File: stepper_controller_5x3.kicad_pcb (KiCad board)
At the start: 2 copper layers, 120.7 x 66 mm, 1 part

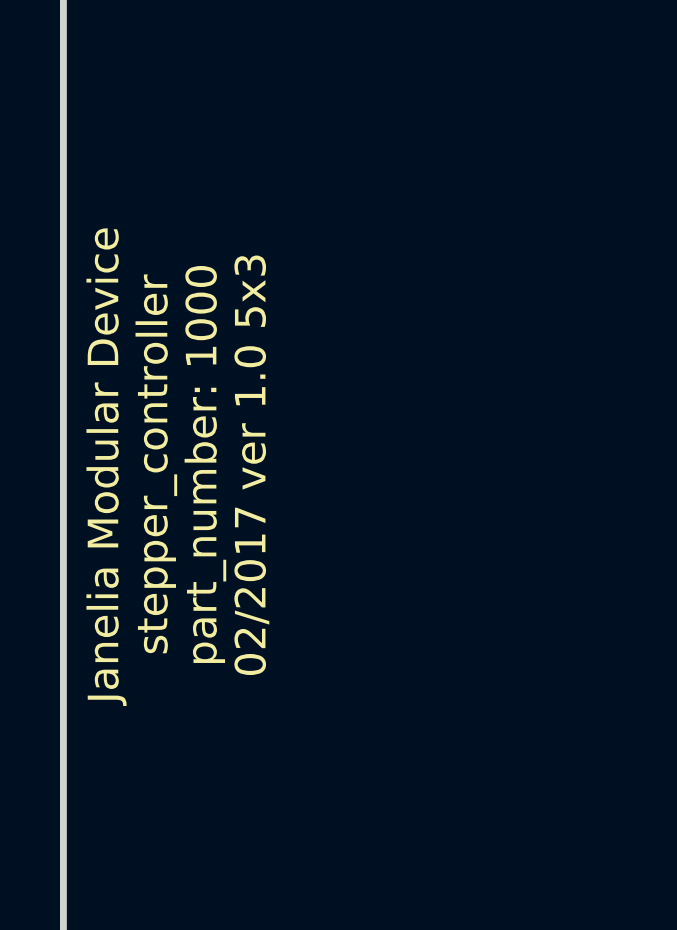
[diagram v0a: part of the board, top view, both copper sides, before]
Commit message: Added files from stepper_controller_3x2.
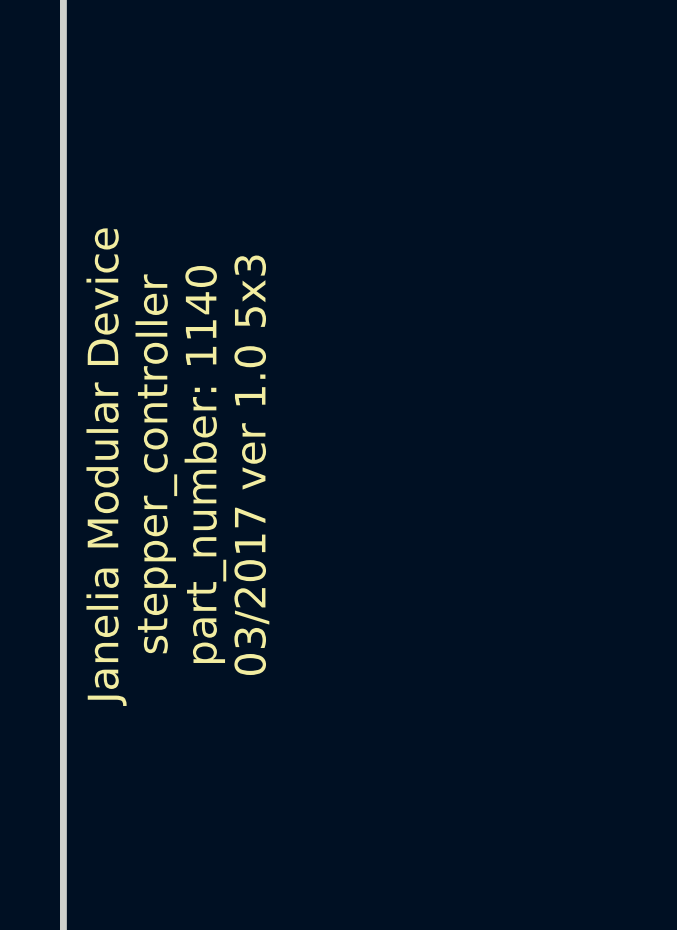
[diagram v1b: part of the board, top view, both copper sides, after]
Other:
- board text added: "Janelia Modular Device stepper_controller part_number: 1140 03/2017 ver 1.0 5x3"
- board text removed: "Janelia Modular Device stepper_controller part_number: 1000 02/2017 ver 1.0 5x3"
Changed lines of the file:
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@@
-(kicad_pcb (version 20170123) (host pcbnew no-vcs-found-7602~57~ubuntu16.04.1)
+(kicad_pcb (version 20170123) (host pcbnew no-vcs-found-40f60c9~58~ubuntu16.04.1)
   (general
     (links 0)
     (no_connects 0)
-    (area 0 0 0 0)
+    (area 69.481699 72.021699 190.868301 138.798301)
     (thickness 1.6)
     (drawings 6)
@@
     (effects (font (size 1.016 1.016) (thickness 0.1905)))
   )
-  (gr_text "Janelia Modular Device\nstepper_controller\npart_number: 1000\n02/2017 ver 1.0 5x3" (at 73.66 105.41 90) (layer F.SilkS)
+  (gr_text "Janelia Modular Device\nstepper_controller\npart_number: 1140\n03/2017 ver 1.0 5x3" (at 73.66 105.41 90) (layer F.SilkS)
     (effects (font (size 1.016 1.016) (thickness 0.254)))
   )

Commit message: Progress towards v1.0.
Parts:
- added C1: 0.1uF, stepper_controller_5x3:SM1210, F.Cu at (283.9, 127.0)
- added C10: 10uF, stepper_controller_5x3:SM1210, F.Cu at (295.1, 100.7)
- added C11: 0.1uF, stepper_controller_5x3:SM1210, F.Cu at (274.4, 102.7)
- added C2: 0.1uF, stepper_controller_5x3:SM1210, F.Cu at (282.9, 138.7)
- added C3: 100uF_POL, stepper_controller_5x3:C_ELEC_12.5, F.Cu at (79.4, 120.7)
- added C4: 10uF, stepper_controller_5x3:SM1210, F.Cu at (224.8, 100.7)
- added C5: 0.1uF, stepper_controller_5x3:SM1210, F.Cu at (204.1, 102.7)
- added C6: 100uF_POL, stepper_controller_5x3:C_ELEC_12.5, F.Cu at (112.4, 120.7)
- added C7: 10uF, stepper_controller_5x3:SM1210, F.Cu at (224.8, 141.6)
- added C8: 0.1uF, stepper_controller_5x3:SM1210, F.Cu at (204.1, 143.6)
- added C9: 100uF_POL, stepper_controller_5x3:C_ELEC_12.5, F.Cu at (145.4, 120.7)
- added CLK1: CLK_32MHZ, stepper_controller_5x3:CTS_SMD_4_7X5MM, F.Cu at (276.6, 128.5)
- added D1: diode_schottky_45V_10A, stepper_controller_5x3:CFP15, F.Cu at (281.4, 117.8)
- added P1: PWR_JACK_2.5x5.5, stepper_controller_5x3:DCJACK_2PIN_HIGHCURRENT, F.Cu at (191.1, 105.4)
- added SS1: STEPSTICK, stepper_controller_5x3:STEPSTICK, F.Cu at (95.2, 105.4)
- added SS2: STEPSTICK, stepper_controller_5x3:STEPSTICK, F.Cu at (128.3, 105.4)
- added SS3: STEPSTICK, stepper_controller_5x3:STEPSTICK, F.Cu at (161.3, 105.4)
- added T1: TERM_BLK_HDR_4POS_VERT_0.2IN, stepper_controller_5x3:TERM_BLK_HDR_4POS_VERT_0.2IN, F.Cu at (95.2, 91.4)
- added T2: TERM_BLK_HDR_4POS_VERT_0.150IN, stepper_controller_5x3:TERM_BLK_HDR_4POS_VERT_0.150IN, F.Cu at (95.2, 120.7)
- added T3: TERM_BLK_HDR_4POS_VERT_0.2IN, stepper_controller_5x3:TERM_BLK_HDR_4POS_VERT_0.2IN, F.Cu at (128.3, 91.4)
- added T4: TERM_BLK_HDR_4POS_VERT_0.150IN, stepper_controller_5x3:TERM_BLK_HDR_4POS_VERT_0.150IN, F.Cu at (128.3, 120.7)
- added T5: TERM_BLK_HDR_4POS_VERT_0.2IN, stepper_controller_5x3:TERM_BLK_HDR_4POS_VERT_0.2IN, F.Cu at (161.3, 91.4)
- added T6: TERM_BLK_HDR_4POS_VERT_0.150IN, stepper_controller_5x3:TERM_BLK_HDR_4POS_VERT_0.150IN, F.Cu at (161.3, 120.0)
- added U1: TMC429, stepper_controller_5x3:QFN-5x5-32, F.Cu at (276.1, 141.4)
- added U2: MAX6817, stepper_controller_5x3:MAX6817, F.Cu at (208.8, 101.8)
- added U3: MAX6817, stepper_controller_5x3:MAX6817, F.Cu at (208.8, 142.7)
- added U4: MAX6817, stepper_controller_5x3:MAX6817, F.Cu at (279.2, 101.8)
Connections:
- MDB1 pad 11: (no net) -> /MOSI
- MDB1 pad 12: (no net) -> /MISO
- MDB1 pad 13: (no net) -> /SCK
- MDB1 pad 15: (no net) -> /CS_429
- MDB1 pad 16: (no net) -> /CS_DRIVER_0
- MDB1 pad 17: (no net) -> /CS_DRIVER_1
- MDB1 pad 18: (no net) -> /CS_DRIVER_2
- MDB1 pad 3V3: (no net) -> +3V3
- MDB1 pad 40: (no net) -> /ENABLE_0
- MDB1 pad 41: (no net) -> /ENABLE_1
- MDB1 pad 42: (no net) -> /ENABLE_2
- MDB1 pad 5: (no net) -> /INT
- MDB1 pad 6: (no net) -> /POSCOMP
- MDB1 pad GND: (no net) -> GND
- MDB1 pad VDD: (no net) -> VDD
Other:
- board size 120.7 x 66 mm -> 121.3 x 67.3 mm
- board text added: "Janelia Modular Device stepper_controller part_number: 1140 06/2017 ver 1.0 5x3"
- board text removed: "Janelia Modular Device stepper_controller part_number: 1140 03/2017 ver 1.0 5x3"

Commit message: Finished v1.0.
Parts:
- C1, C10, C11, C2, C4, C5, C7, C8, CLK1, D1, U1, U2, U3, U4: moved to B.Cu
- C3, C6, C9: value 100uF_POL -> 220uF_POL; footprint stepper_controller_5x3:C_ELEC_12.5 -> stepper_controller_5x3:C_ELEC_10
- moved C10 203.7 mm to (91.4, 96.5)
- moved C11 182.3 mm to (94.0, 128.3), turned to 90 degrees
- moved U4 182.0 mm to (99.1, 128.3), turned to 270 degrees
- moved C2 176.5 mm to (108.0, 115.6), turned to 90 degrees
- moved U1 162.6 mm to (115.6, 115.6), turned to 180 degrees
- moved C1 151.7 mm to (132.7, 115.6), turned to 270 degrees
- moved CLK1 151.4 mm to (125.7, 115.6), turned to 180 degrees
- moved C7 110.0 mm to (124.5, 96.5)
- moved D1 104.1 mm to (179.1, 98.4)
- moved C8 78.6 mm to (127.0, 128.3), turned to 90 degrees
- moved U3 78.1 mm to (132.1, 128.3), turned to 270 degrees
- moved C3 72.7 mm to (148.6, 98.4)
- moved SS1 70.2 mm to (165.1, 98.4)
- moved T1 70.2 mm to (165.1, 84.5)
- moved T2 69.9 mm to (165.1, 123.8)
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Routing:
- net GND: track 0.00 -> 385.3 mm
- net +3V3: track 0.00 -> 308.9 mm
- net /MOSI: track 0.00 -> 150.8 mm
- net /MISO: track 0.00 -> 148.3 mm
- net VDD: track 0.00 -> 145.3 mm
- net /SCK: track 0.00 -> 138.1 mm
- net /CS_DRIVER_0: track 0.00 -> 79.8 mm
- net /ENABLE_0: track 0.00 -> 76.9 mm
- net /tmc429_driver_0/REFR_0: track 0.00 -> 74.8 mm
- net /INT: track 0.00 -> 73.6 mm, vias 0 -> 2
- net /ENABLE_2: track 0.00 -> 73.2 mm
- net /CS_DRIVER_1: track 0.00 -> 72.7 mm
- net /tmc429_driver_0/DIR_0: track 0.00 -> 71.9 mm, vias 0 -> 1
- net /tmc429_driver_0/STEP_0: track 0.00 -> 66.3 mm, vias 0 -> 1
- net /tmc429_driver_0/REF_0: track 0.00 -> 57.3 mm
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- added copper zone on B.Cu, net GND
- added copper zone on F.Cu, net VDD
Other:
- net class GND: trace_width 0.4064 -> 0.3048
- net class POWER: clearance 0.254 -> 0.1016; trace_width 0.8128 -> 0.3048
- net class SIGNAL: trace_width 0.4064 -> 0.3048
- net class SUPERPOWER: clearance 0.254 -> 0.1016; trace_width 1.2192 -> 1.27
- board text added: "0"
- board text added: "1"
- board text added: "2"
- board text added: "2.5x5.5 Center + +9-42VDC"
- board text added: "A+"
- board text added: "A-"
- board text added: "B+"
- board text added: "B-"
- board text added: "GND"
- board text added: "REF"
- board text added: "REFR"

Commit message: Progress toward v1.1.
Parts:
- added L1: 90nH, stepper_controller_5x3:ECS-MPI4040, B.Cu at (172.7, 87.8)
- added L10: 90nH, stepper_controller_5x3:ECS-MPI4040, B.Cu at (101.6, 87.8)
- added L11: 90nH, stepper_controller_5x3:ECS-MPI4040, B.Cu at (96.5, 87.8)
- added L12: 90nH, stepper_controller_5x3:ECS-MPI4040, B.Cu at (91.4, 87.8)
- added L2: 90nH, stepper_controller_5x3:ECS-MPI4040, B.Cu at (167.6, 87.8)
- added L3: 90nH, stepper_controller_5x3:ECS-MPI4040, B.Cu at (162.6, 87.8)
- added L4: 90nH, stepper_controller_5x3:ECS-MPI4040, B.Cu at (157.5, 87.8)
- added L5: 90nH, stepper_controller_5x3:ECS-MPI4040, B.Cu at (139.7, 87.8)
- added L6: 90nH, stepper_controller_5x3:ECS-MPI4040, B.Cu at (134.6, 87.8)
- added L7: 90nH, stepper_controller_5x3:ECS-MPI4040, B.Cu at (129.5, 87.8)
- added L8: 90nH, stepper_controller_5x3:ECS-MPI4040, B.Cu at (124.5, 87.8)
- added L9: 90nH, stepper_controller_5x3:ECS-MPI4040, B.Cu at (106.7, 87.8)
- added R1: 470pF, stepper_controller_5x3:SM0805, B.Cu at (172.7, 80.6)
- added R10: 470pF, stepper_controller_5x3:SM0805, B.Cu at (101.6, 80.6)
- added R11: 470pF, stepper_controller_5x3:SM0805, B.Cu at (96.5, 80.6)
- added R12: 470pF, stepper_controller_5x3:SM0805, B.Cu at (91.4, 80.6)
- added R2: 470pF, stepper_controller_5x3:SM0805, B.Cu at (167.6, 80.6)
- added R3: 470pF, stepper_controller_5x3:SM0805, B.Cu at (162.6, 80.6)
- added R4: 470pF, stepper_controller_5x3:SM0805, B.Cu at (157.5, 80.6)
- added R5: 470pF, stepper_controller_5x3:SM0805, B.Cu at (139.7, 80.6)
- added R6: 470pF, stepper_controller_5x3:SM0805, B.Cu at (134.6, 80.6)
- added R7: 470pF, stepper_controller_5x3:SM0805, B.Cu at (129.5, 80.6)
- added R8: 470pF, stepper_controller_5x3:SM0805, B.Cu at (124.5, 80.6)
- added R9: 470pF, stepper_controller_5x3:SM0805, B.Cu at (106.7, 80.6)
- moved C10 0.64 mm to (91.4, 97.2)
- moved C3 0.64 mm to (148.6, 99.1)
- moved C4 0.64 mm to (157.5, 97.2)
- moved C6 0.64 mm to (115.6, 99.1)
- moved C7 0.64 mm to (124.5, 97.2)
- moved C9 0.64 mm to (82.5, 99.1)
- moved SS1 0.64 mm to (165.1, 99.1)
- moved SS2 0.64 mm to (132.1, 99.1)
- moved SS3 0.64 mm to (99.1, 99.1)
- moved T1 0.64 mm to (165.1, 83.8)
- moved T3 0.64 mm to (132.1, 83.8)
- moved T5 0.64 mm to (99.1, 83.8)
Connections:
- MDB1 pad 14: (no net) -> Net-(MDB1-Pad14)
- MDB1 pad 19: (no net) -> Net-(MDB1-Pad19)
- MDB1 pad 2: (no net) -> Net-(MDB1-Pad2)
- MDB1 pad 20: (no net) -> Net-(MDB1-Pad20)
- MDB1 pad 21: (no net) -> Net-(MDB1-Pad21)
- MDB1 pad 22: (no net) -> Net-(MDB1-Pad22)
- MDB1 pad 23: (no net) -> Net-(MDB1-Pad23)
- MDB1 pad 29: (no net) -> Net-(MDB1-Pad29)
- MDB1 pad 30: (no net) -> Net-(MDB1-Pad30)
- MDB1 pad 33: (no net) -> Net-(MDB1-Pad33)
- MDB1 pad 34: (no net) -> Net-(MDB1-Pad34)
- MDB1 pad 35: (no net) -> Net-(MDB1-Pad35)
- MDB1 pad 36: (no net) -> Net-(MDB1-Pad36)
- MDB1 pad 37: (no net) -> Net-(MDB1-Pad37)
- MDB1 pad 38: (no net) -> Net-(MDB1-Pad38)
- MDB1 pad 43: (no net) -> Net-(MDB1-Pad43)
- MDB1 pad 44: (no net) -> Net-(MDB1-Pad44)
- MDB1 pad 45: (no net) -> Net-(MDB1-Pad45)
- MDB1 pad 46: (no net) -> Net-(MDB1-Pad46)
- MDB1 pad 47: (no net) -> Net-(MDB1-Pad47)
- MDB1 pad 48: (no net) -> Net-(MDB1-Pad48)
- MDB1 pad 49: (no net) -> Net-(MDB1-Pad49)
- MDB1 pad 50: (no net) -> Net-(MDB1-Pad50)
- MDB1 pad 51: (no net) -> Net-(MDB1-Pad51)
- MDB1 pad 52: (no net) -> Net-(MDB1-Pad52)
- MDB1 pad 53: (no net) -> Net-(MDB1-Pad53)
- MDB1 pad 54: (no net) -> Net-(MDB1-Pad54)
- MDB1 pad 55: (no net) -> Net-(MDB1-Pad55)
- MDB1 pad A10: (no net) -> Net-(MDB1-PadA10)
- MDB1 pad A11: (no net) -> Net-(MDB1-PadA11)
- MDB1 pad AGND: (no net) -> Net-(MDB1-PadAGND)
- MDB1 pad AREF: (no net) -> Net-(MDB1-PadAREF)
- MDB1 pad DAC0: (no net) -> Net-(MDB1-PadDAC0)
- MDB1 pad DAC1: (no net) -> Net-(MDB1-PadDAC1)
- MDB1 pad VEE: (no net) -> VEE
- T1 pad 1: /tmc429_driver_0/stepper_0/B_- -> /tmc429_driver_0/stepper_0/B_-F
- T1 pad 2: /tmc429_driver_0/stepper_0/B_+ -> /tmc429_driver_0/stepper_0/B_+F
- T1 pad 3: /tmc429_driver_0/stepper_0/A_- -> /tmc429_driver_0/stepper_0/A_-F
- T1 pad 4: /tmc429_driver_0/stepper_0/A_+ -> /tmc429_driver_0/stepper_0/A_+F
- T3 pad 1: /tmc429_driver_0/stepper_1/B_- -> /tmc429_driver_0/stepper_1/B_-F
- T3 pad 2: /tmc429_driver_0/stepper_1/B_+ -> /tmc429_driver_0/stepper_1/B_+F
- T3 pad 3: /tmc429_driver_0/stepper_1/A_- -> /tmc429_driver_0/stepper_1/A_-F
- T3 pad 4: /tmc429_driver_0/stepper_1/A_+ -> /tmc429_driver_0/stepper_1/A_+F
- T5 pad 1: /tmc429_driver_0/stepper_2/B_- -> /tmc429_driver_0/stepper_2/B_-F
- T5 pad 2: /tmc429_driver_0/stepper_2/B_+ -> /tmc429_driver_0/stepper_2/B_+F
- T5 pad 3: /tmc429_driver_0/stepper_2/A_- -> /tmc429_driver_0/stepper_2/A_-F
- T5 pad 4: /tmc429_driver_0/stepper_2/A_+ -> /tmc429_driver_0/stepper_2/A_+F
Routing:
- net GND: track 385.3 -> 0.00 mm
- net +3V3: track 308.9 -> 0.00 mm
- net /MOSI: track 150.8 -> 0.00 mm
- net /MISO: track 148.3 -> 0.00 mm
- net VDD: track 145.3 -> 0.00 mm
- net /SCK: track 138.1 -> 0.00 mm
- net /CS_DRIVER_0: track 79.8 -> 0.00 mm
- net /ENABLE_0: track 76.9 -> 0.00 mm
- net /tmc429_driver_0/REFR_0: track 74.8 -> 0.00 mm
- net /INT: track 73.6 -> 0.00 mm, vias 2 -> 0
- net /ENABLE_2: track 73.2 -> 0.00 mm
- net /CS_DRIVER_1: track 72.7 -> 0.00 mm
- net /tmc429_driver_0/DIR_0: track 71.9 -> 0.00 mm, vias 1 -> 0
- net /tmc429_driver_0/STEP_0: track 66.3 -> 0.00 mm, vias 1 -> 0
- net /tmc429_driver_0/REF_0: track 57.3 -> 0.00 mm
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- removed copper zone on B.Cu, net GND
- removed copper zone on F.Cu, net VDD
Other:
- board text added: "2.5x5.5 Center + +12-42VDC"
- board text added: "Janelia Modular Device stepper_controller part_number: 1140 10/2017 ver 1.1 5x3"
- board text removed: "2.5x5.5 Center + +9-42VDC"
- board text removed: "Janelia Modular Device stepper_controller part_number: 1140 06/2017 ver 1.0 5x3"

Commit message: More progress towards v1.1.
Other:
- board text added: "2.5x5.5 Center + +12-30VDC"
- board text removed: "2.5x5.5 Center + +12-42VDC"
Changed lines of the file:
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@@
-(kicad_pcb (version 20170922) (host pcbnew no-vcs-found-9bd5522~60~ubuntu16.04.1)
+(kicad_pcb (version 20170922) (host pcbnew no-vcs-found-a562525~60~ubuntu16.04.1)
 (general
   (thickness 1.6)
@@
     )
   )
-  (gr_text "2.5x5.5\nCenter +\n+12-42VDC" (at 184.785 114.935) (layer F.SilkS)
+  (gr_text "2.5x5.5\nCenter +\n+12-30VDC" (at 184.785 114.935) (layer F.SilkS)
     (effects (font (size 1.016 1.016) (thickness 0.254)))
   )

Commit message: Finished version 1.1.
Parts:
- removed R10, R11, R12, R2, R3, R4, R5, R6, R7, R8, R9: 470pF, stepper_controller_5x3:SM0805
- added C12: 0.1uF, stepper_controller_5x3:SM1210, B.Cu at (170.8, 128.3)
- added C13: 220uF_POL, stepper_controller_5x3:C_ELEC_10, F.Cu at (115.6, 99.1)
- added C14: 10uF, stepper_controller_5x3:SM1210, B.Cu at (124.5, 97.2)
- added C15: 470pF, stepper_controller_5x3:SM0805, B.Cu at (138.4, 79.4)
- added C16: 470pF, stepper_controller_5x3:SM0805, B.Cu at (135.9, 79.4)
- added C17: 470pF, stepper_controller_5x3:SM0805, B.Cu at (128.3, 79.4)
- added C18: 470pF, stepper_controller_5x3:SM0805, B.Cu at (125.7, 79.4)
- added C19: 0.1uF, stepper_controller_5x3:SM1210, B.Cu at (137.8, 128.3)
- added C20: 220uF_POL, stepper_controller_5x3:C_ELEC_10, F.Cu at (82.5, 99.1)
- added C21: 10uF, stepper_controller_5x3:SM1210, B.Cu at (91.4, 97.2)
- added C22: 470pF, stepper_controller_5x3:SM0805, B.Cu at (105.4, 79.4)
- added C23: 470pF, stepper_controller_5x3:SM0805, B.Cu at (102.9, 79.4)
- added C24: 470pF, stepper_controller_5x3:SM0805, B.Cu at (95.2, 79.4)
- added C25: 470pF, stepper_controller_5x3:SM0805, B.Cu at (92.7, 79.4)
- added C26: 0.1uF, stepper_controller_5x3:SM1210, B.Cu at (104.8, 128.3)
- added REG1: CONV_DC_DC_5V_1A, stepper_controller_5x3:DC_DC_CONV_R78C, F.Cu at (76.2, 123.2)
- added RV1: VAR, stepper_controller_5x3:SM0805, B.Cu at (170.2, 81.9)
- added RV10: VAR, stepper_controller_5x3:SM0805, B.Cu at (133.3, 79.4)
- added RV11: VAR, stepper_controller_5x3:SM0805, B.Cu at (130.8, 79.4)
- added RV12: VAR, stepper_controller_5x3:SM0805, B.Cu at (123.2, 79.4)
- added RV13: VAR, stepper_controller_5x3:SM0805, B.Cu at (104.1, 81.9)
- added RV14: VAR, stepper_controller_5x3:SM0805, B.Cu at (94.0, 81.9)
- added RV15: VAR, stepper_controller_5x3:SM0805, B.Cu at (108.0, 79.4)
- added RV16: VAR, stepper_controller_5x3:SM0805, B.Cu at (100.3, 79.4)
- added RV17: VAR, stepper_controller_5x3:SM0805, B.Cu at (97.8, 79.4)
- added RV18: VAR, stepper_controller_5x3:SM0805, B.Cu at (90.2, 79.4)
- added RV2: VAR, stepper_controller_5x3:SM0805, B.Cu at (160.0, 81.9)
- added RV3: VAR, stepper_controller_5x3:SM0805, B.Cu at (174.0, 79.4)
- added RV4: VAR, stepper_controller_5x3:SM0805, B.Cu at (166.4, 79.4)
- added RV5: VAR, stepper_controller_5x3:SM0805, B.Cu at (163.8, 79.4)
- added RV6: VAR, stepper_controller_5x3:SM0805, B.Cu at (156.2, 79.4)
- added RV7: VAR, stepper_controller_5x3:SM0805, B.Cu at (137.2, 81.9)
- added RV8: VAR, stepper_controller_5x3:SM0805, B.Cu at (127.0, 81.9)
- added RV9: VAR, stepper_controller_5x3:SM0805, B.Cu at (141.0, 79.4)
- added U5: MAX6817, stepper_controller_5x3:MAX6817, B.Cu at (99.1, 128.3)
- C10: value 10uF -> 470pF; footprint stepper_controller_5x3:SM1210 -> stepper_controller_5x3:SM0805
- C11, C8: value 0.1uF -> 470pF; footprint stepper_controller_5x3:SM1210 -> stepper_controller_5x3:SM0805
- C2: value 0.1uF -> 10uF
- C3: value 220uF_POL -> 10uF; footprint stepper_controller_5x3:C_ELEC_10 -> stepper_controller_5x3:SM1210; moved to B.Cu
- C4: value 10uF -> 0.1uF
- C9: value 220uF_POL -> 470pF; footprint stepper_controller_5x3:C_ELEC_10 -> stepper_controller_5x3:SM0805; moved to B.Cu
- R1: value 470pF -> 1k; footprint stepper_controller_5x3:SM0805 -> stepper_controller_5x3:SM1210
- U2: value MAX6817 -> SN74ABT541BDWR; footprint stepper_controller_5x3:MAX6817 -> stepper_controller_5x3:SOIC_20
- moved D1 105.8 mm to (73.7, 89.5)
- moved R1 101.9 mm to (77.5, 116.8), turned to 180 degrees
- moved C9 88.6 mm to (168.9, 79.4)
- moved C11 81.2 mm to (158.8, 79.4)
- moved U2 77.5 mm to (89.5, 114.3), turned to 90 degrees
- moved C3 74.1 mm to (77.5, 120.0), turned to 180 degrees
- moved C10 72.1 mm to (161.3, 79.4), turned to 90 degrees
- moved C8 66.1 mm to (171.4, 79.4)
- moved C5 63.2 mm to (98.4, 114.3), turned to 270 degrees
- moved C4 52.4 mm to (108.0, 114.3), turned to 90 degrees
- moved C2 34.7 mm to (74.9, 126.4), turned to 0 degrees
- moved C6 33.0 mm to (148.6, 99.1)
- moved U4 33.0 mm to (132.1, 128.3)
- moved C7 33.0 mm to (157.5, 97.2)
- moved U3 33.0 mm to (165.1, 128.3)
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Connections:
- C10 pad 1: VDD -> /tmc429_driver_0/stepper_0/B_+F
- C11 pad 1: +3V3 -> /tmc429_driver_0/stepper_0/B_-F
- C2 pad 1: +3V3 -> VAA
- C3 pad 1: VDD -> +5V
- C4 pad 1: VDD -> +3V3
- C5 pad 1: +3V3 -> +5V
- C6 pad 1: VDD -> VAA
- C7 pad 1: VDD -> VAA
- C8 pad 1: +3V3 -> /tmc429_driver_0/stepper_0/A_+F
- C9 pad 1: VDD -> /tmc429_driver_0/stepper_0/A_-F
- MDB1 pad 14: Net-(MDB1-Pad14) -> (no net)
- MDB1 pad 19: Net-(MDB1-Pad19) -> (no net)
- MDB1 pad 2: Net-(MDB1-Pad2) -> (no net)
- MDB1 pad 20: Net-(MDB1-Pad20) -> (no net)
- MDB1 pad 21: Net-(MDB1-Pad21) -> (no net)
- MDB1 pad 22: Net-(MDB1-Pad22) -> (no net)
- MDB1 pad 23: Net-(MDB1-Pad23) -> +5V
- MDB1 pad 29: Net-(MDB1-Pad29) -> (no net)
- MDB1 pad 30: Net-(MDB1-Pad30) -> (no net)
- MDB1 pad 33: Net-(MDB1-Pad33) -> (no net)
- MDB1 pad 34: Net-(MDB1-Pad34) -> (no net)
- MDB1 pad 35: Net-(MDB1-Pad35) -> (no net)
- MDB1 pad 36: Net-(MDB1-Pad36) -> (no net)
- MDB1 pad 37: Net-(MDB1-Pad37) -> (no net)
- MDB1 pad 38: Net-(MDB1-Pad38) -> (no net)
- MDB1 pad 43: Net-(MDB1-Pad43) -> (no net)
- MDB1 pad 44: Net-(MDB1-Pad44) -> (no net)
- MDB1 pad 45: Net-(MDB1-Pad45) -> (no net)
- MDB1 pad 46: Net-(MDB1-Pad46) -> (no net)
- MDB1 pad 47: Net-(MDB1-Pad47) -> (no net)
- MDB1 pad 48: Net-(MDB1-Pad48) -> (no net)
- MDB1 pad 49: Net-(MDB1-Pad49) -> (no net)
- MDB1 pad 50: Net-(MDB1-Pad50) -> (no net)
- MDB1 pad 51: Net-(MDB1-Pad51) -> (no net)
- MDB1 pad 52: Net-(MDB1-Pad52) -> (no net)
- MDB1 pad 53: Net-(MDB1-Pad53) -> (no net)
- MDB1 pad 54: Net-(MDB1-Pad54) -> (no net)
- MDB1 pad 55: Net-(MDB1-Pad55) -> (no net)
- MDB1 pad A10: Net-(MDB1-PadA10) -> (no net)
- MDB1 pad A11: Net-(MDB1-PadA11) -> (no net)
- MDB1 pad AGND: Net-(MDB1-PadAGND) -> (no net)
- MDB1 pad AREF: Net-(MDB1-PadAREF) -> (no net)
- MDB1 pad DAC0: Net-(MDB1-PadDAC0) -> (no net)
- MDB1 pad DAC1: Net-(MDB1-PadDAC1) -> (no net)
- MDB1 pad VEE: VEE -> (no net)
- R1 pad 1: /tmc429_driver_0/stepper_0/A_+F -> +5V
- SS1 pad 15: +3V3 -> +5V
- SS1 pad 5: /CS_DRIVER_0 -> /tmc429_driver_0/~CS_DRIVER_0_B
- SS1 pad 6: /SCK -> /tmc429_driver_0/SCK_B
- SS1 pad 7: /MOSI -> /tmc429_driver_0/MOSI_B
- SS1 pad 8: /ENABLE_0 -> /tmc429_driver_0/~ENABLE_0_B
- SS1 pad 9: VDD -> VAA
- SS2 pad 15: +3V3 -> +5V
- SS2 pad 5: /CS_DRIVER_1 -> /tmc429_driver_0/~CS_DRIVER_1_B
- SS2 pad 6: /SCK -> /tmc429_driver_0/SCK_B
- SS2 pad 7: /MOSI -> /tmc429_driver_0/MOSI_B
- SS2 pad 8: /ENABLE_1 -> /tmc429_driver_0/~ENABLE_1_B
- SS2 pad 9: VDD -> VAA
- SS3 pad 15: +3V3 -> +5V
- SS3 pad 5: /CS_DRIVER_2 -> /tmc429_driver_0/~CS_DRIVER_2_B
- SS3 pad 6: /SCK -> /tmc429_driver_0/SCK_B
- SS3 pad 7: /MOSI -> /tmc429_driver_0/MOSI_B
- SS3 pad 8: /ENABLE_2 -> /tmc429_driver_0/~ENABLE_2_B
- SS3 pad 9: VDD -> VAA
- U2 pad 1: /tmc429_driver_0/stepper_0/REF_B -> GND
- U2 pad 2: GND -> /SCK
- U2 pad 3: /tmc429_driver_0/stepper_0/REFR_B -> /MOSI
- U2 pad 4: /tmc429_driver_0/REFR_0 -> /ENABLE_0
- U2 pad 5: +3V3 -> /CS_DRIVER_0
- U2 pad 6: /tmc429_driver_0/REF_0 -> /ENABLE_1
- U3 pad 1: /tmc429_driver_0/stepper_1/REF_B -> /tmc429_driver_0/stepper_0/REF_B
- U3 pad 3: /tmc429_driver_0/stepper_1/REFR_B -> /tmc429_driver_0/stepper_0/REFR_B
- U3 pad 4: /tmc429_driver_0/REFR_1 -> /tmc429_driver_0/REFR_0
- U3 pad 6: /tmc429_driver_0/REF_1 -> /tmc429_driver_0/REF_0
- U4 pad 1: /tmc429_driver_0/stepper_2/REF_B -> /tmc429_driver_0/stepper_1/REF_B
- U4 pad 3: /tmc429_driver_0/stepper_2/REFR_B -> /tmc429_driver_0/stepper_1/REFR_B
- U4 pad 4: /tmc429_driver_0/REFR_2 -> /tmc429_driver_0/REFR_1
- U4 pad 6: /tmc429_driver_0/REF_2 -> /tmc429_driver_0/REF_1
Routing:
- net GND: track 0.00 -> 495.6 mm
- net VAA: track 0.00 -> 177.3 mm
- net +3V3: track 0.00 -> 166.9 mm, vias 0 -> 4
- net /MOSI: track 0.00 -> 160.0 mm, vias 0 -> 2
- net +5V: track 0.00 -> 152.2 mm, vias 0 -> 1
- net /MISO: track 0.00 -> 146.9 mm, vias 0 -> 1
- net /INT: track 0.00 -> 117.0 mm, vias 0 -> 1
- net /tmc429_driver_0/DIR_0: track 0.00 -> 98.3 mm
- net /tmc429_driver_0/STEP_0: track 0.00 -> 94.2 mm
- net /tmc429_driver_0/~CS_DRIVER_0_B: track 0.00 -> 88.5 mm, vias 0 -> 1
- net /tmc429_driver_0/SCK_B: track 0.00 -> 81.2 mm
- net /tmc429_driver_0/MOSI_B: track 0.00 -> 79.3 mm
- net /tmc429_driver_0/~ENABLE_0_B: track 0.00 -> 77.6 mm, vias 0 -> 1
- net /POSCOMP: track 0.00 -> 61.7 mm
- net /tmc429_driver_0/REFR_0: track 0.00 -> 61.6 mm, vias 0 -> 2
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- added copper zone on B.Cu, net GND
- added copper zone on F.Cu, net VAA
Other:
- net class SUPERPOWER: trace_width 1.27 -> 1.0668
- board text added: "5V"
- board text added: "Disconnect Motor Driver Power Before Unplugging Motor Connectors"
- board text added: "Motor Driver Power 2.5x5.5 Center + +12-30VDC"
- board text removed: "2.5x5.5 Center + +12-30VDC"

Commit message: Changes towards v1.2
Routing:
- net GND: track 495.6 -> 0.00 mm
- net VAA: track 177.3 -> 0.00 mm
- net +3V3: track 166.9 -> 0.00 mm, vias 4 -> 0
- net /MOSI: track 160.0 -> 0.00 mm, vias 2 -> 0
- net +5V: track 152.2 -> 0.00 mm, vias 1 -> 0
- net /MISO: track 146.9 -> 0.00 mm, vias 1 -> 0
- net /INT: track 117.0 -> 0.00 mm, vias 1 -> 0
- net /tmc429_driver_0/DIR_0: track 98.3 -> 0.00 mm
- net /tmc429_driver_0/STEP_0: track 94.2 -> 0.00 mm
- net /tmc429_driver_0/~CS_DRIVER_0_B: track 88.5 -> 0.00 mm, vias 1 -> 0
- net /tmc429_driver_0/SCK_B: track 81.2 -> 0.00 mm
- net /tmc429_driver_0/MOSI_B: track 79.3 -> 0.00 mm
- net /tmc429_driver_0/~ENABLE_0_B: track 77.6 -> 0.00 mm, vias 1 -> 0
- net /POSCOMP: track 61.7 -> 0.00 mm
- net /tmc429_driver_0/REFR_0: track 61.6 -> 0.00 mm, vias 2 -> 0
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- removed copper zone on B.Cu, net GND
- removed copper zone on F.Cu, net VAA
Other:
- board text added: "Janelia Modular Device stepper_controller part_number: 1140 03/2019 ver 1.2 5x3"
- board text removed: "Janelia Modular Device stepper_controller part_number: 1140 10/2017 ver 1.1 5x3"
